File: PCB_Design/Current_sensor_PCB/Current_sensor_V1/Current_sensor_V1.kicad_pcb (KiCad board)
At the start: 2 copper layers, 24 parts, among them J1 Screw_Terminal_01x02, J2 Barrel_Jack_Switch, J3 Conn_Coaxial, J4 Conn_Coaxial, J5 Conn_Coaxial, U1 CASR_6-NP

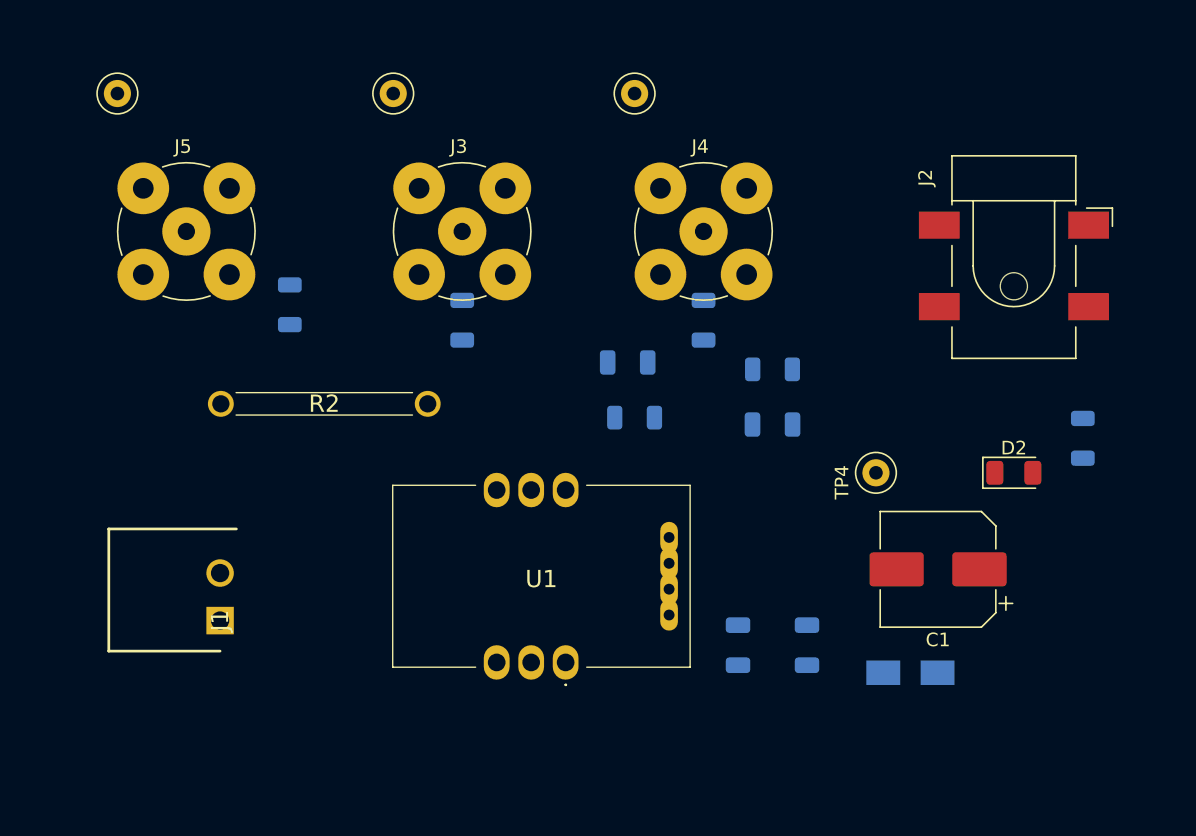
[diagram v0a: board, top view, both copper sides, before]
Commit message: Finished Current sensor V1 PCB
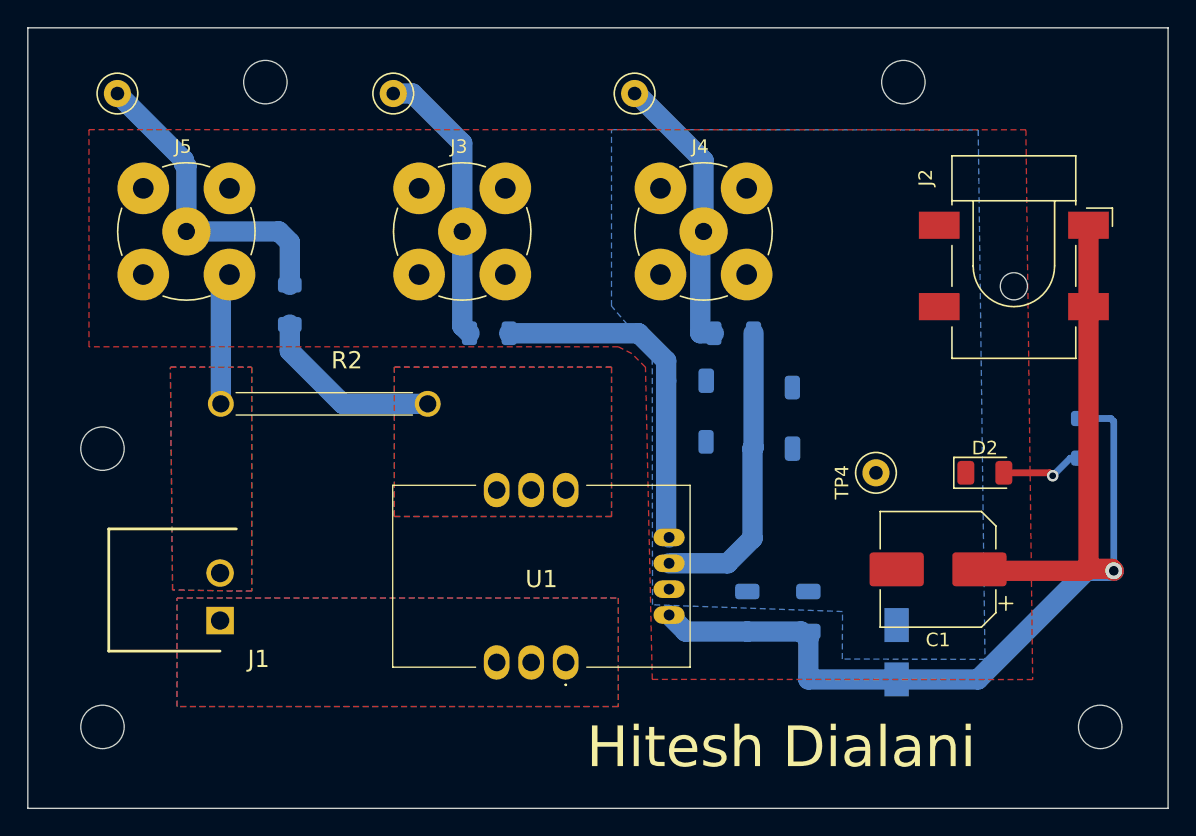
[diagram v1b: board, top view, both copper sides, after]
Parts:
- added H1: MountingHole, MountingHole:MountingHole_3.2mm_M3, F.Cu at (37.0, 143.0)
- added H2: MountingHole, MountingHole:MountingHole_3.2mm_M3, F.Cu at (37.0, 163.5)
- added H3: MountingHole, MountingHole:MountingHole_3.2mm_M3, F.Cu at (96.0, 116.0)
- added H4: MountingHole, MountingHole:MountingHole_3.2mm_M3, F.Cu at (49.0, 116.0)
- added H5: MountingHole, MountingHole:MountingHole_3.2mm_M3, F.Cu at (110.5, 163.5)
- J1: value Screw_Terminal_01x02 -> 284512-2
- moved C4 4.51 mm to (80.0, 138.0)
- moved R4 4.20 mm to (80.0, 142.5)
- moved C3 2.57 mm to (84.5, 155.0)
- moved C2 2.48 mm to (89.0, 155.0)
- moved R7 2.42 mm to (83.5, 134.5), turned to 180 degrees
- moved R6 2.22 mm to (65.5, 134.5), turned to 180 degrees
- moved D2 2.14 mm to (102.0, 144.8)
- moved D1 1.82 mm to (95.5, 158.0), turned to 90 degrees
- moved C5 1.78 mm to (86.4, 143.0)
- moved R5 1.34 mm to (86.4, 138.5)
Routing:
- net +5V: track 0.00 -> 88.5 mm, vias 0 -> 1
- net /V_Ref: track 0.00 -> 25.5 mm
- net /Shunt_terminated: track 0.00 -> 23.4 mm
- net /V_Out: track 0.00 -> 22.1 mm
- net /V_Out_terminated: track 0.00 -> 20.9 mm
- net /V_Ref_terminated: track 0.00 -> 20.8 mm
- net /Shunt_current: track 0.00 -> 13.7 mm
- net GND: track 0.00 -> 9.79 mm
- net Net-(D2-Pad2): track 0.00 -> 6.45 mm, vias 0 -> 1
- added copper zone on B.Cu, net /Current_in
- added copper zone on F.Cu, net /Current_in
- added copper zone on B.Cu, net /Shunt_current
- added copper zone on F.Cu, net /Shunt_current
- added copper zone on B.Cu, net GND
- added copper zone on F.Cu, net GND
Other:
- board outline added: 84 x 57.5 mm
- board text added: "Hitesh Dialani"
